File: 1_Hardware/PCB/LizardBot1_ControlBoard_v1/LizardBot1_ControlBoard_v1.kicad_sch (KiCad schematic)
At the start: 0 parts

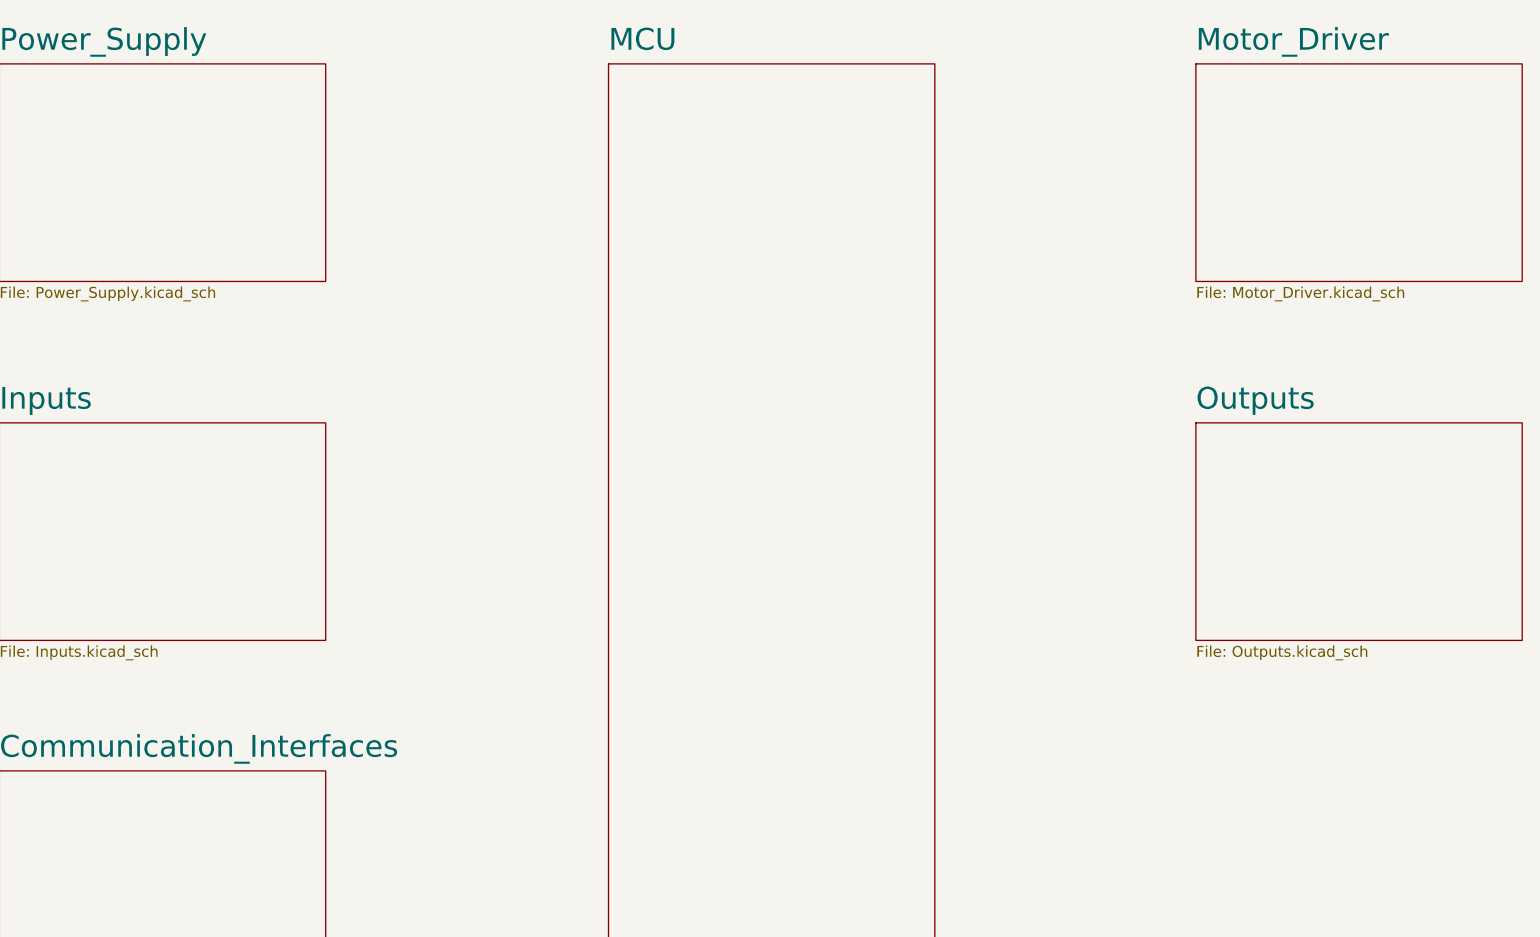
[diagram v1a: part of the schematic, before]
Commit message: Added Motor_Driver schematic.
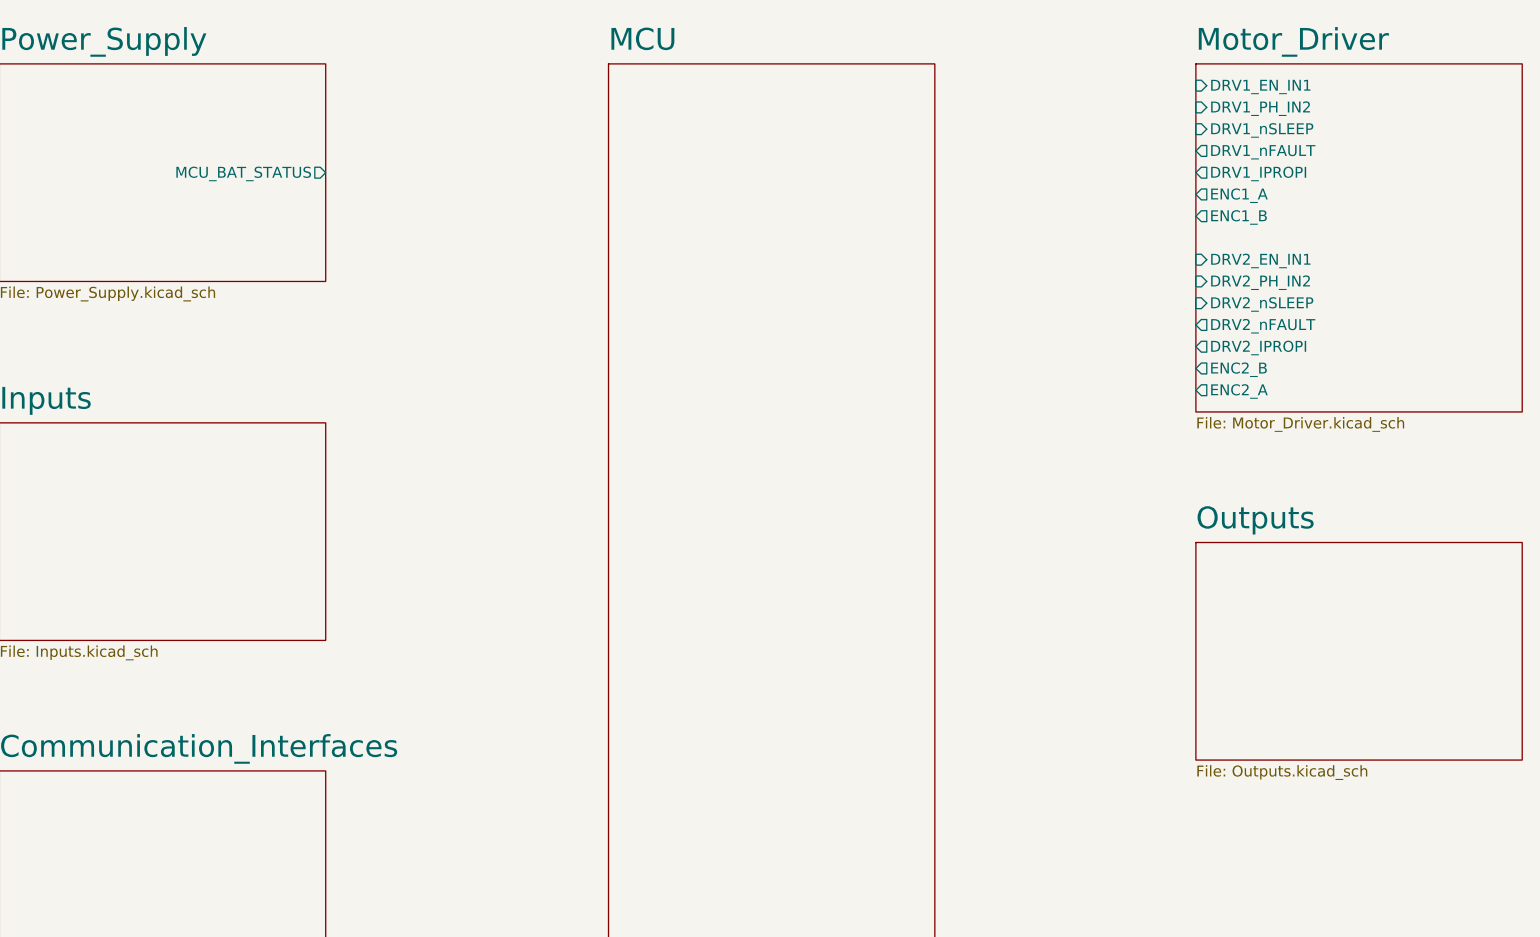
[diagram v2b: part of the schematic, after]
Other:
- sheet Motor_Driver ports: added DRV1_EN_IN1, DRV1_IPROPI, DRV1_PH_IN2, DRV1_nFAULT, DRV1_nSLEEP, DRV2_EN_IN1, DRV2_IPROPI, DRV2_PH_IN2, DRV2_nFAULT, DRV2_nSLEEP, ENC1_A, ENC1_B, ENC2_A, ENC2_B; removed none
- sheet Power_Supply ports: added MCU_BAT_STATUS; removed none
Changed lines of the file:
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@@
 	(title_block
 		(title "LizardBot 1 Control Board: Hierarchical Sheet")
-		(date "2024-06-17")
+		(date "2024-06-21")
 		(rev "v1.0.0")
 		(company "Lizard Electronics")
@@
 			)
 		)
+		(pin "MCU_BAT_STATUS" output
+			(at 92.71 40.64 0)
+			(effects
+				(font
+					(size 1.27 1.27)
+				)
+				(justify right)
+			)
+		)
 		(instances
 			(project "LizardBot1_ControlBoard_v1"
@@
 	(sheet
 		(at 194.31 27.94)
-		(size 38.1 25.4)
+		(size 38.1 40.64)
 		(fields_autoplaced yes)
 		(stroke
@@
 		)
 		(property "Sheetfile" "Motor_Driver.kicad_sch"
-			(at 194.31 53.9246 0)
-			(effects
-				(font
-					(size 1.27 1.27)
-				)
-				(justify left top)
-			)
-		)
-		(instances
-			(project "LizardBot1_ControlBoard_v1"
-				(path "/1a674a4d-d877-4d7a-ad57-e0a054705c31"
-					(page "5")
+			(at 194.31 69.1646 0)
+			(effects
+				(font
+					(size 1.27 1.27)
+				)
+				(justify left top)
+			)
+		)
+		(pin "DRV1_IPROPI" output
+			(at 194.31 40.64 180)
+			(effects
+				(font
+					(size 1.27 1.27)
+				)
+				(justify left)
+			)
+		)
+		(pin "DRV1_nFAULT" output
+			(at 194.31 38.1 180)
+			(effects
+				(font
+					(size 1.27 1.27)
+				)
+				(justify left)
+			)
+		)
+		(pin "DRV2_PH_IN2" input
+			(at 194.31 53.34 180)
+			(effects
+				(font
+					(size 1.27 1.27)
+				)
+				(justify left)
+			)
+		)
+		(pin "DRV2_EN_IN1" input
+			(at 194.31 50.8 180)
+			(effects
+				(font
+					(size 1.27 1.27)
+				)
+				(justify left)
+			)
+		)
+		(pin "DRV2_nSLEEP" input
+			(at 194.31 55.88 180)
+			(effects
+				(font
+					(size 1.27 1.27)
+				)
+				(justify left)
+			)
+		)
+		(pin "DRV1_EN_IN1" input
+			(at 194.31 30.48 180)
+			(effects
+				(font
+					(size 1.27 1.27)
+				)
+				(justify left)
+			)
+		)
+		(pin "DRV1_PH_IN2" input
+			(at 194.31 33.02 180)
+			(effects
+				(font
+					(size 1.27 1.27)
+				)
+				(justify left)
+			)
+		)
+		(pin "DRV1_nSLEEP" input
+			(at 194.31 35.56 180)
+			(effects
+				(font
+					(size 1.27 1.27)
+				)
+				(justify left)
+			)
+		)
+		(pin "DRV2_IPROPI" output
+			(at 194.31 60.96 180)
+			(effects
+				(font
+					(size 1.27 1.27)
+				)
+				(justify left)
+			)
+		)
+		(pin "DRV2_nFAULT" output
+			(at 194.31 58.42 180)
+			(effects
+				(font
+					(size 1.27 1.27)
+				)
+				(justify left)
+			)
+		)
+		(pin "ENC2_B" output
+			(at 194.31 63.5 180)
+			(effects
+				(font
+					(size 1.27 1.27)
+				)
+				(justify left)
+			)
+		)
+		(pin "ENC2_A" output
+			(at 194.31 66.04 180)
+			(effects
+				(font
+					(size 1.27 1.27)
+				)
+				(justify left)
+			)
+		)
+		(pin "ENC1_A" output
+			(at 194.31 43.18 180)
+			(effects
+				(font
+					(size 1.27 1.27)
+				)
+				(justify left)
+			)
+		)
+		(pin "ENC1_B" output
+			(at 194.31 45.72 180)
+			(effects
+				(font
+					(size 1.27 1.27)
+				)
+				(justify left)
+			)
+		)
+		(instances
+			(project "LizardBot1_ControlBoard_v1"
+				(path "/1a674a4d-d877-4d7a-ad57-e0a054705c31"
+					(page "4")
 				)
 			)
@@
 			(project "LizardBot1_ControlBoard_v1"
 				(path "/1a674a4d-d877-4d7a-ad57-e0a054705c31"
-					(page "6")
+					(page "5")
 				)
 			)
@@
 	)
 	(sheet
-		(at 194.31 69.85)
+		(at 194.31 83.82)
 		(size 38.1 25.4)
 		(fields_autoplaced yes)
@@
 		)
 		(property "Sheetname" "Outputs"
-			(at 194.31 68.5034 0)
+			(at 194.31 82.4734 0)
 			(effects
 				(font
@@
 		)
 		(property "Sheetfile" "Outputs.kicad_sch"
-			(at 194.31 95.8346 0)
-			(effects
-				(font
-					(size 1.27 1.27)
-				)
-				(justify left top)
-			)
-		)
-		(instances
-			(project "LizardBot1_ControlBoard_v1"
-				(path "/1a674a4d-d877-4d7a-ad57-e0a054705c31"
-					(page "7")
+			(at 194.31 109.8046 0)
+			(effects
+				(font
+					(size 1.27 1.27)
+				)
+				(justify left top)
+			)
+		)
+		(instances
+			(project "LizardBot1_ControlBoard_v1"
+				(path "/1a674a4d-d877-4d7a-ad57-e0a054705c31"
+					(page "6")
 				)
 			)
@@
 			(project "LizardBot1_ControlBoard_v1"
 				(path "/1a674a4d-d877-4d7a-ad57-e0a054705c31"
-					(page "4")
-				)
-			)
+					(page "7")
+				)
+			)

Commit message: Added MCU schematic
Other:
- sheet MCU ports: added DRV1_EN_IN1, DRV1_IPROPI, DRV1_PH_IN2, DRV1_nFAULT, DRV1_nSLEEP, DRV2_EN_IN1, DRV2_IPROPI, DRV2_PH_IN2, DRV2_nFAULT, DRV2_nSLEEP, ENC1_A, ENC1_B, ENC2_A, ENC2_B, MCU_BAT_STATUS, MCU_BUTTON, MCU_BUZZER, MCU_FAN_PWM, MCU_NEOPIXEL, MCU_RXD0, MCU_SCL, MCU_SDA, MCU_TXD0; removed none
